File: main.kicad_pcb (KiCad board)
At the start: 2 copper layers, 228.6 x 70.6 mm, 134 parts, among them J1 Conn_02x16_Row_Letter_First, J10 Conn_01x26_Pin, J11 Conn_ARM_JTAG_SWD_10, J2 Conn_01x05, J3 Conn_01x02, J4 Screw_Terminal_01x02, J5 Screw_Terminal_01x10, J6 Screw_Terminal_01x10, J7 Screw_Terminal_01x02, J8 Screw_Terminal_01x10, J9 Screw_Terminal_01x10, U10 TLP3558A, U11 TLP3558A, U12 TLP3558A, U13 TLP3558A, U14 TLP3558A, U15 TLP3558A, U16 TLP3558A, U17 TLP3558A, U18 TLP3558A, U19 TLP3558A, U2 NCP1117-3.3_TO252, U20 TLP3558A, U21 TLP3558A, U22 TLP3558A, U23 TLP3558A, U24 TLP3558A, U25 TLP3558A, U26 TLP3558A, U27 TLP3558A, U28 TLP3558A, U29 TLP3558A, U3 STM32G070KBT6, U30 TLP3558A, U31 TLP3558A, U32 TLP3558A, U33 TLP3558A, U34 TLP3558A, U35 TLP3558A, U36 TLP3558A, U37 TLP3558A, U38 TLP3558A, U39 TLP3558A, U4 TLP3558A, U40 TLP3558A, U41 TLP3558A, U42 TLP3558A, U43 TLP3558A, U44 TLP3558A, U45 TLP3558A, U46 TLP3558A, U47 TLP3558A, U5 TLP3558A, U6 TLP3558A, U7 TLP3558A, U8 TLP3558A, U9 TLP3558A

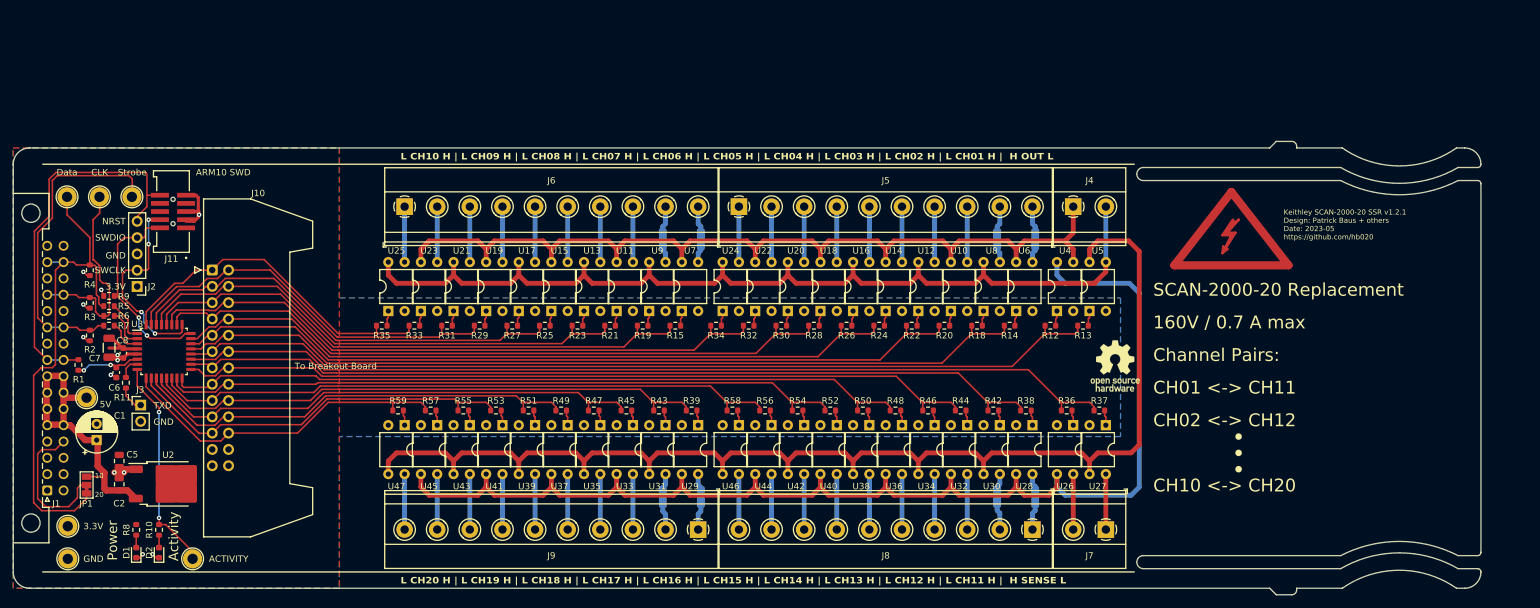
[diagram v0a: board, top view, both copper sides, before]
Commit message: Revised barriers, modified the PCB to comply with related standards, rerouted traces.
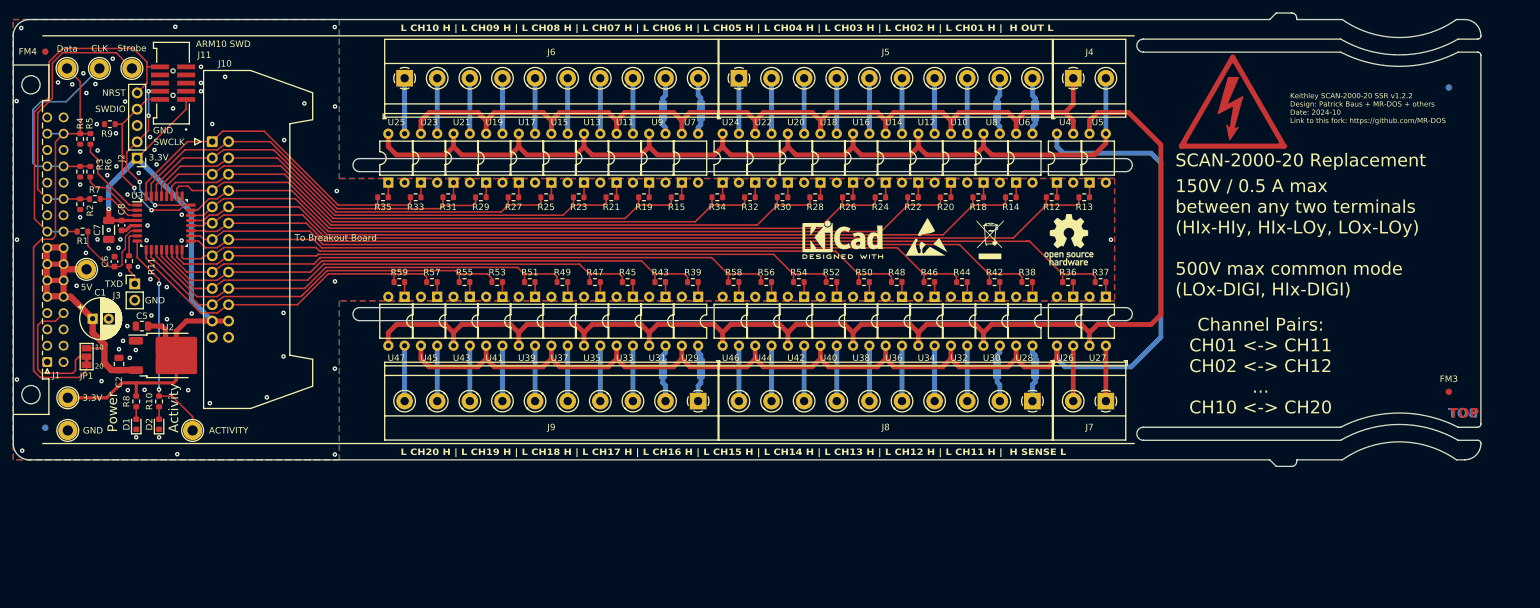
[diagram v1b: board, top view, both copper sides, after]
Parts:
- added FM1: Fiducial, Fiducial:Fiducial_1mm_Mask2mm, B.Cu at (30.4, 91.8)
- added FM2: Fiducial, Fiducial:Fiducial_1mm_Mask2mm, B.Cu at (249.0, 38.8)
- added FM3: Fiducial, Fiducial:Fiducial_1mm_Mask2mm, F.Cu at (249.0, 86.3)
- added FM4: Fiducial, Fiducial:Fiducial_1mm_Mask2mm, F.Cu at (30.4, 33.3)
- added REF**: ESD-Logo_6.6x6mm_SilkScreen, Symbol:ESD-Logo_6.6x6mm_SilkScreen, F.Cu at (167.7, 62.1)
- added REF**: KiCad-Logo2_5mm_SilkScreen, Symbol:KiCad-Logo2_5mm_SilkScreen, F.Cu at (154.6, 62.6)
- added REF**: WEEE-Logo_4.2x6mm_SilkScreen, Symbol:WEEE-Logo_4.2x6mm_SilkScreen, F.Cu at (177.6, 62.6)
- SYM1: footprint Symbol:Symbol_Highvoltage_Type2_CopperTop_Small -> Symbol:Symbol_HighVoltage_Triangle_17x15mm_Copper
- moved R9 26.8 mm to (40.5, 44.6)
- moved R5 26.2 mm to (37.4, 46.9), turned to 90 degrees
- moved R6 22.7 mm to (37.4, 52.0), turned to 90 degrees
- moved SYM1 21.7 mm to (215.3, 41.0)
- moved C5 21.3 mm to (45.5, 76.0), turned to 180 degrees
- moved LOGO2 20.9 mm to (189.8, 62.6)
- moved R1 20.8 mm to (36.2, 61.3), turned to 180 degrees
- moved R4 20.5 mm to (35.8, 46.9)
- moved R2 20.5 mm to (35.8, 57.0)
- moved R3 20.5 mm to (35.8, 52.0)
- moved R12 20.0 mm to (187.1, 55.9)
- moved R13 20.0 mm to (192.2, 55.9)
- moved R14 20.0 mm to (180.8, 55.9)
- moved R15 20.0 mm to (128.7, 55.9)
- moved R18 20.0 mm to (175.7, 55.9)
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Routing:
- net +3.3V: track 6.78 -> 100.4 mm, vias 0 -> 1
- net GND: track 30.3 -> 2.98 mm, vias 12 -> 75
- net /DATA: track 77.3 -> 67.5 mm
- net /Microcontroller/DATA: track 6.44 -> 13.2 mm
- net /STROBE: track 49.6 -> 43.5 mm
- net Net-(U3-NRST): track 10.2 -> 15.8 mm, vias 2 -> 0
- net /Relays/Input pins/Bus_HIGH: track 194.1 -> 199.0 mm
- net /Relays/Input pins/Bus_LOW: track 192.0 -> 196.6 mm
- net +5V: track 45.7 -> 50.1 mm
- net /Microcontroller/CLK: track 6.17 -> 9.92 mm
- net /~{NRST}: track 60.6 -> 57.4 mm
- net /Microcontroller/SWCLK: track 31.1 -> 28.2 mm
- net /CLK: track 32.4 -> 30.5 mm
- net /Microcontroller/SWDIO: track 32.2 -> 30.3 mm
- net /Microcontroller/STROBE: track 5.06 -> 6.83 mm
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- added copper zone on F.Cu, net GND
- removed copper zone on F.Cu, net +3.3V
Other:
- outline, holes or cut-outs redrawn
- rule pad_to_mask_clearance: 0 -> 0.2
- board text added: "0"
- board text added: "0 mm"
- board text added: "0.01 mm"
- board text added: "0.02"
- board text added: "0.035 mm"
- board text added: "0.2000 mm"
- board text added: "0.2000 mm / 0.2500 mm"
- board text added: "1"
- board text added: "1.5 mm"
- board text added: "1.5900 mm"
- board text added: "150V / 0.5 A max between any two terminals (HIx-HIy, HIx-LOy, LOx-LOy) 500V max common mode (LOx-DIGI, HIx-DIGI)"
- board text added: "2"
- board text added: "228.6000 mm x 70.6120 mm"
- board text added: "3.3"
- board text added: "4.5"
- board text added: "B.Cu"
- board text added: "B.Mask"
- board text added: "B.Paste"
- board text added: "B.Silkscreen"
- board text added: "BOARD CHARACTERISTICS"
- board text added: "BOT"
- board text added: "Barriers design: A) Digital - LO: 500V peak, functional insulation (2.5 mm AC, 2 mm CD) AC General: IPC-2221B external: 2.5 mm AC: UL796 + UL60950-1: 1.6 mm CD: UL60950-1 PD 1 MG I: 2 mm B) HI - LO: 160V peak, functional insulation (1.25 mm AC, 0.75 mm CD) AC General: IPC-2221B external: 1.25 mm (violated, rating reduced to 150 V) AC: UL796 + UL60950-1: 0.625 mm CD: UL60950-1 PD 1 MG I: 0.75 mm C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"
- board text added: "Board Thickness:"
- board text added: "Board overall dimensions:"
- board text added: "Bottom Silk Screen"
- board text added: "Bottom Solder Mask"
- board text added: "Bottom Solder Paste"
- board text added: "C"
- board text added: "Castellated pads:"
- board text added: "Channel Pairs: CH01 <-> CH11 CH02 <-> CH12 ... CH10 <-> CH20"
- board text added: "Color"
- board text added: "Copper Finish:"
- board text added: "Copper Layer Count:"
- board text added: "Dielectric 1"
- board text added: "Do not place any components above this line"
- board text added: "Do not place any components below this line"
- board text added: "Edge card connectors:"
- board text added: "Epsilon R"
- board text added: "F.Cu"
- board text added: "F.Mask"
- board text added: "F.Paste"
- board text added: "F.Silkscreen"
- board text added: "FR4"
- board text added: "FR4 natural"
- board text added: "Green"
- board text added: "HAL SnPb"
- board text added: "Impedance Control:"
- board text added: "Keithley SCAN-2000-20 SSR v1.2.2 Design: Patrick Baus + MR-DOS + others Date: 2024-10 Link to this fork: https://github.com/MR-DOS"
- board text added: "Layer Name"
- board text added: "Loss Tangent"
- board text added: "Material"
- board text added: "Min hole diameter:"
- board text added: "Min track/spacing:"
- board text added: "No"
- board text added: "Not specified"
- board text added: "PCB Manufacturing Instructions: - Panel thickness: Approximate - Copper thickness on outer layers: Minimum final after plating - Insulation material: Recommended - Insulation material thickness: Recommended - Insulation material dielectric constant: Approximate - Flammability: Use only UL94 V-0 materials Assembly instructions: - Clean to meet IPC J-STD-001E, Class 2 after assembly Testing instruc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"
- board text added: "Plated Board Edge:"
- board text added: "TOP"
- board text added: "Thickness (mm)"
- board text added: "Top Silk Screen"
- board text added: "Top Solder Mask"
- board text added: "Top Solder Paste"
- board text added: "Type"
- board text added: "White"
- board text added: "copper"
- board text added: "core"
- board text removed: "160V / 0.7 A max"
- board text removed: "CH01 <-> CH11"
- board text removed: "CH02 <-> CH12"
- board text removed: "CH10 <-> CH20"
- board text removed: "Channel Pairs:"
- board text removed: "Keithley SCAN-2000-20 SSR v1.2.1 Design: Patrick Baus + others Date: 2023-05 https://github.com/hb020"
- board text removed: "Manufacturing Instruction: - Material FR-4 - Finished thickness: 1.57 mm ± 0.13 mm - Surface finish: ENIG - Solder mask color: Blue - PCBs are to be RoHS compliant - Do not edit artwork, e.g. to add logos or order numbers - Clean to meet IPC J-STD-001E, Class 2 after assembly"
- board text removed: "No not place any components above this line"
- board text removed: "No not place any components below this line"
- board text removed: "Note: Drawn on a 10 mil grid."
